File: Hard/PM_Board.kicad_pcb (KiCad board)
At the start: 2 copper layers, 70 x 70 mm, 75 parts, among them J1 Micro_SD_Card_Det_Hirose_DM3AT, J101 LiPo_V+, J102 LiPo_V-, J2 KRC_Conn_SWD, J3 USB_B_Micro, J4 KRC_Conn_CAN, J5 KRC_Conn_CAN, J6 KRC_Conn_CAN, Q1 SSM6J501NU, Q2 2n7002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

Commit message: [update] パターンを編集完了
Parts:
- moved C24 28.1 mm to (137.2, 90.4), turned to 180 degrees
- moved C15 26.1 mm to (148.3, 84.6)
- moved R8 26.1 mm to (156.1, 80.2)
- moved U2 26.1 mm to (150.6, 82.0)
- moved R9 26.1 mm to (156.1, 82.4)
- moved C16 26.1 mm to (154.6, 81.3)
- moved R10 26.1 mm to (157.8, 81.3)
- moved C25 18.9 mm to (138.8, 99.5), turned to 180 degrees
- moved C26 14.9 mm to (141.7, 103.5)
- moved D4 11.3 mm to (156.2, 88.5), turned to 270 degrees
- moved Q1 4.05 mm to (124.0, 106.5)
- moved Q2 4.05 mm to (130.9, 106.5)
- moved R13 4.05 mm to (126.6, 108.2)
- moved R14 4.05 mm to (132.4, 109.0)
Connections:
- C17 pad 1: Net-(C17-Pad1) -> VCC
- C19 pad 1: Net-(C17-Pad1) -> VCC
- J101 pad 1: Net-(D4-Pad2) -> +BATT
- Q1 pad 4: Net-(C17-Pad1) -> VCC
- Q1 pad 8: Net-(C17-Pad1) -> VCC
- R10 pad 1: VCC -> +BATT
- R10 pad 2: Net-(C17-Pad1) -> Net-(D4-Pad2)
- R13 pad 1: Net-(C17-Pad1) -> VCC
- R8 pad 1: VCC -> +BATT
- R9 pad 1: Net-(C17-Pad1) -> Net-(D4-Pad2)
- U2 pad 8: VCC -> +BATT
- VR1 pad 1: Net-(C17-Pad1) -> VCC
- VR1 pad 3: Net-(C17-Pad1) -> VCC
- VR2 pad 1: Net-(C17-Pad1) -> VCC
- VR2 pad 3: Net-(C17-Pad1) -> VCC
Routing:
- net Net-(C17-Pad1): track 54.4 -> 0.00 mm
- net VCC: track 116.9 -> 156.6 mm, vias 0 -> 2
- net /INA226_SCL: track 37.0 -> 51.0 mm
- net +BATT: track 0.00 -> 11.3 mm
- net +3V3: track 134.8 -> 144.6 mm
- net /INA226_SDA: track 38.5 -> 46.0 mm
- net /INA226_Alert: track 40.1 -> 45.5 mm
- net Net-(D4-Pad2): track 6.71 -> 1.40 mm
- net /Power_Cutoff: track 22.5 -> 18.6 mm, vias 2 -> 0
- net GND: vias 134 -> 138
- added copper zone on F.Cu, net +BATT
- removed copper zone on F.Cu, net Net-(C17-Pad1)

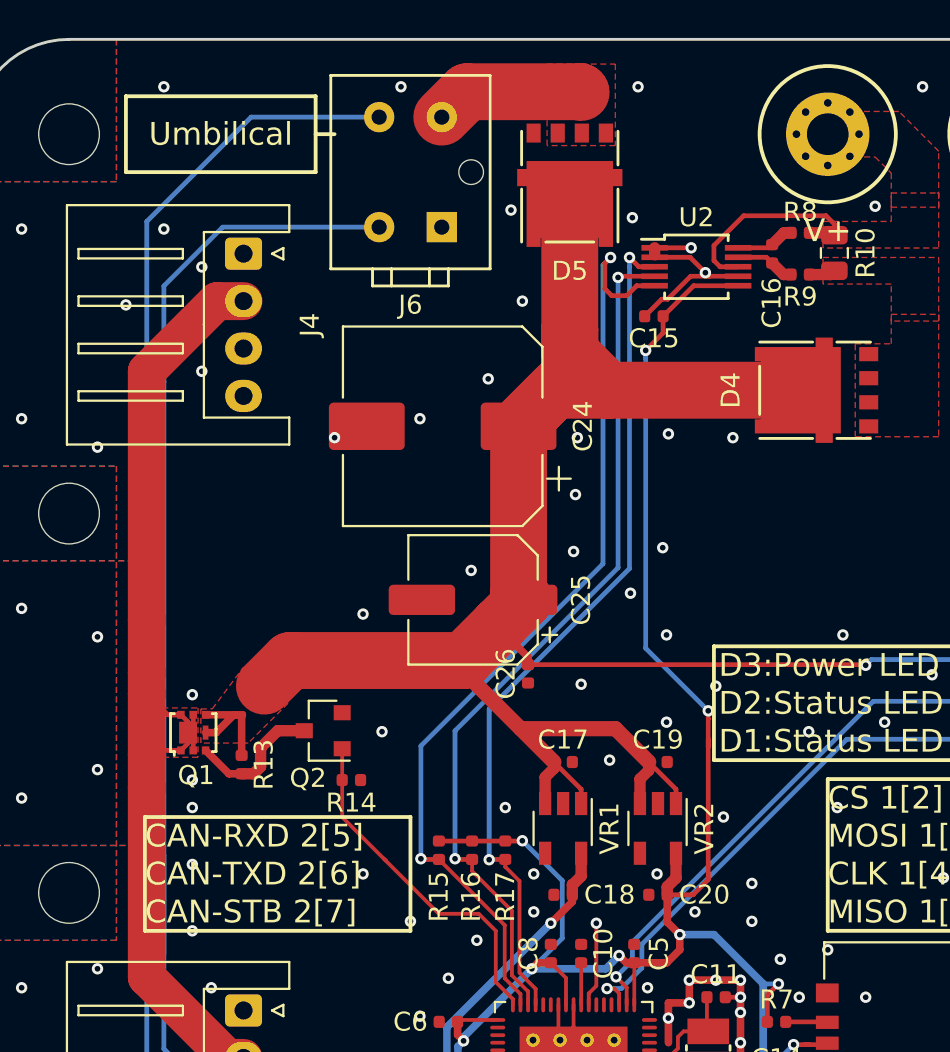
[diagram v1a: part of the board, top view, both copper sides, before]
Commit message: [update] アンビリカルをDF1Eに変更
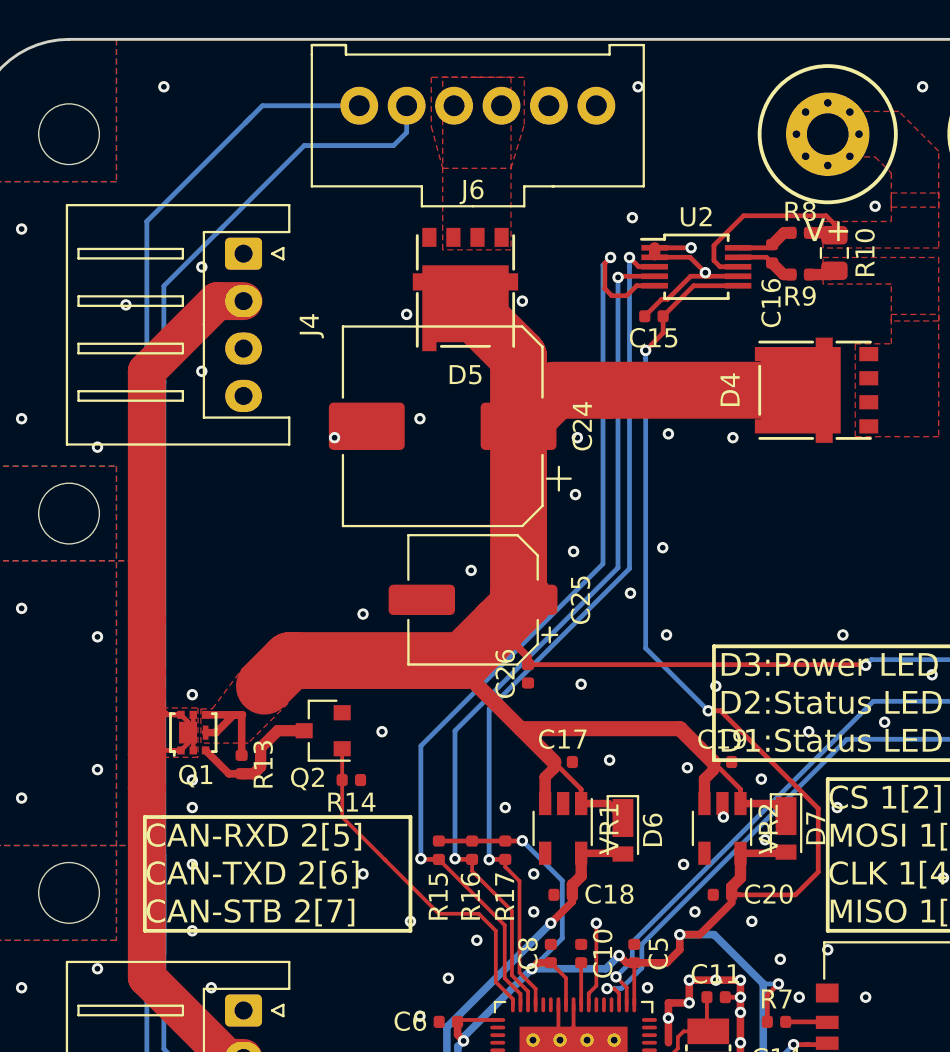
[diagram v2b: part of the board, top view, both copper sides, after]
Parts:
- added D6: RSX101VA, Diode_SMD:D_TUMD2, F.Cu at (146.7, 111.7)
- added D7: RSX101VA, Diode_SMD:D_TUMD2, F.Cu at (155.3, 111.6)
- J6: value KRC_Conn_CAN -> Umbilical; footprint KUTKiCad_footprint:Hirose_DF33-DF33C-4DP-3.3DSA_2x02_P3.3_Vertical -> KUTKiCad_footprint:Hirose_DF1E_DF1E-6P-2.5DS_1x06_P2.5mm_Vertical
- moved J6 10.4 mm to (145.3, 73.5), turned to 180 degrees
- moved D5 7.78 mm to (138.4, 83.9)
- moved C19 3.40 mm to (151.9, 108.1)
- moved C20 3.40 mm to (151.9, 115.1)
- moved VR2 3.40 mm to (151.9, 111.6)
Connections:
- J6 pad 2: Net-(D5-Pad2) -> GND
- J6 pad 3: /CAN_H -> Net-(D5-Pad2)
- J6 pad 4: /CAN_L -> Net-(D5-Pad2)
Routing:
- net +3V3: track 144.6 -> 153.0 mm
- net Net-(D5-Pad2): track 7.92 -> 0.00 mm
- net /CAN_H: track 77.2 -> 82.5 mm
- net +5V: track 22.9 -> 25.1 mm
- net VCC: track 156.6 -> 155.7 mm
- net GND: vias 138 -> 136
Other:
- board text removed: "Umbilical"

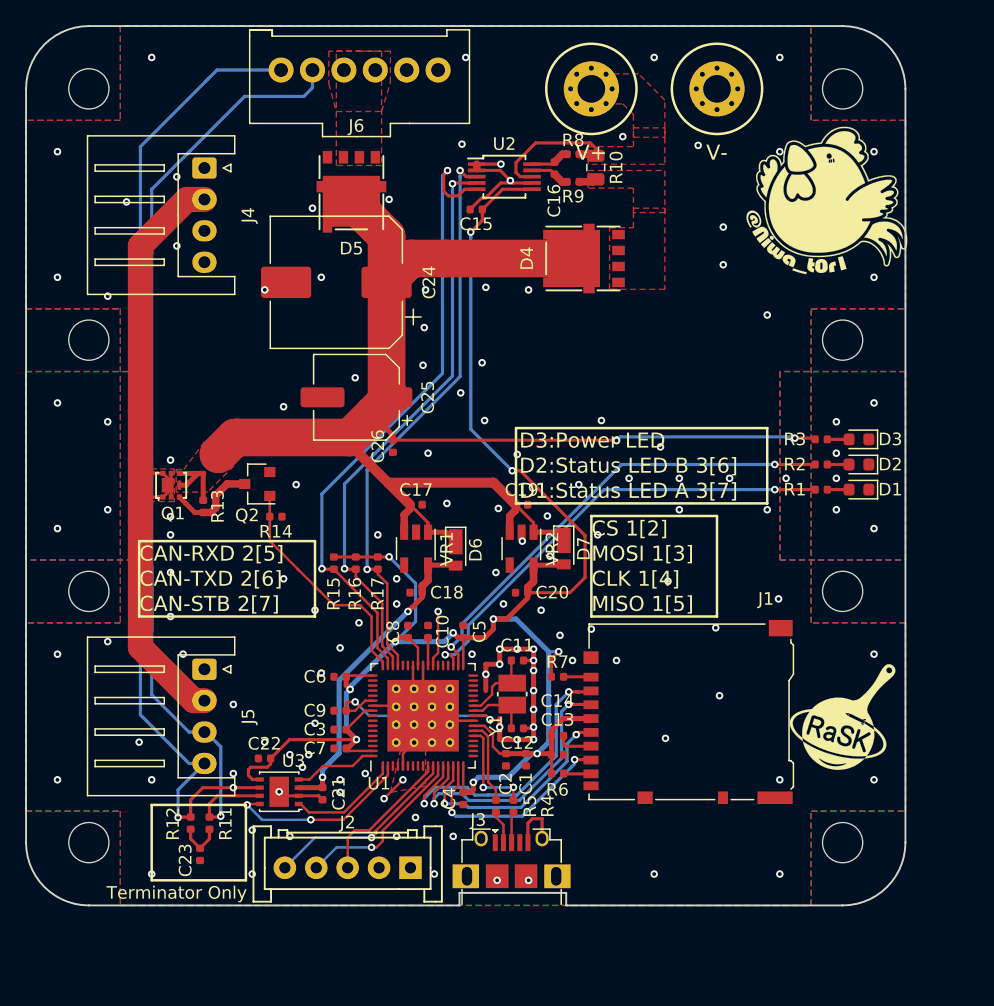
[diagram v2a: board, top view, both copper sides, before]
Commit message: [update] 部品の干渉を修正
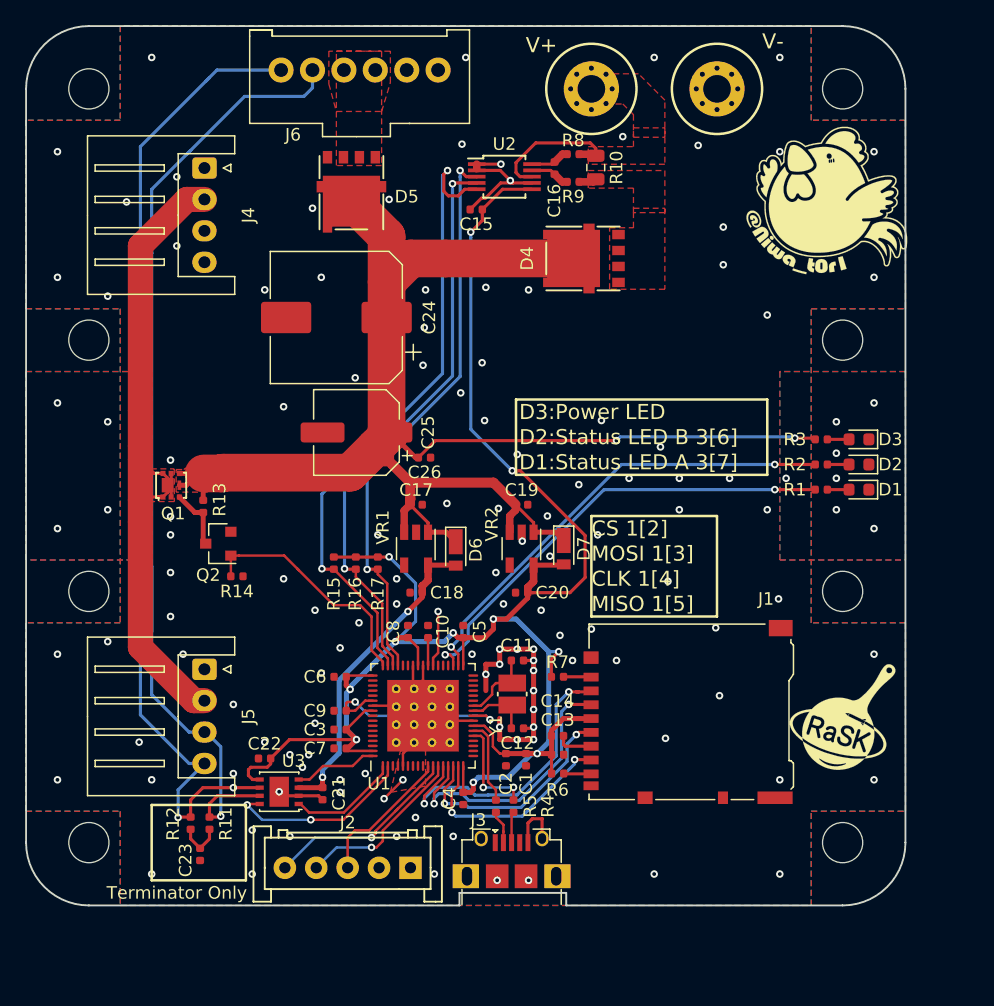
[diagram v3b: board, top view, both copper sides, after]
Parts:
- moved Q2 5.67 mm to (127.8, 111.2)
- moved R14 5.67 mm to (129.3, 113.8)
- moved C24 2.80 mm to (137.2, 93.2)
- moved C25 2.80 mm to (138.8, 102.3)
- moved C26 2.67 mm to (144.2, 104.3), turned to 180 degrees
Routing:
- net Net-(Q1-Pad3): track 7.24 -> 4.97 mm
- net /Power_Cutoff: track 18.6 -> 19.3 mm
- net GND: vias 136 -> 134
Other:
- board text removed: "CAN-RXD 2[5]"
- board text removed: "CAN-STB 2[7]"
- board text removed: "CAN-TXD 2[6]"

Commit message: [update] SDカード用のLDOを追加
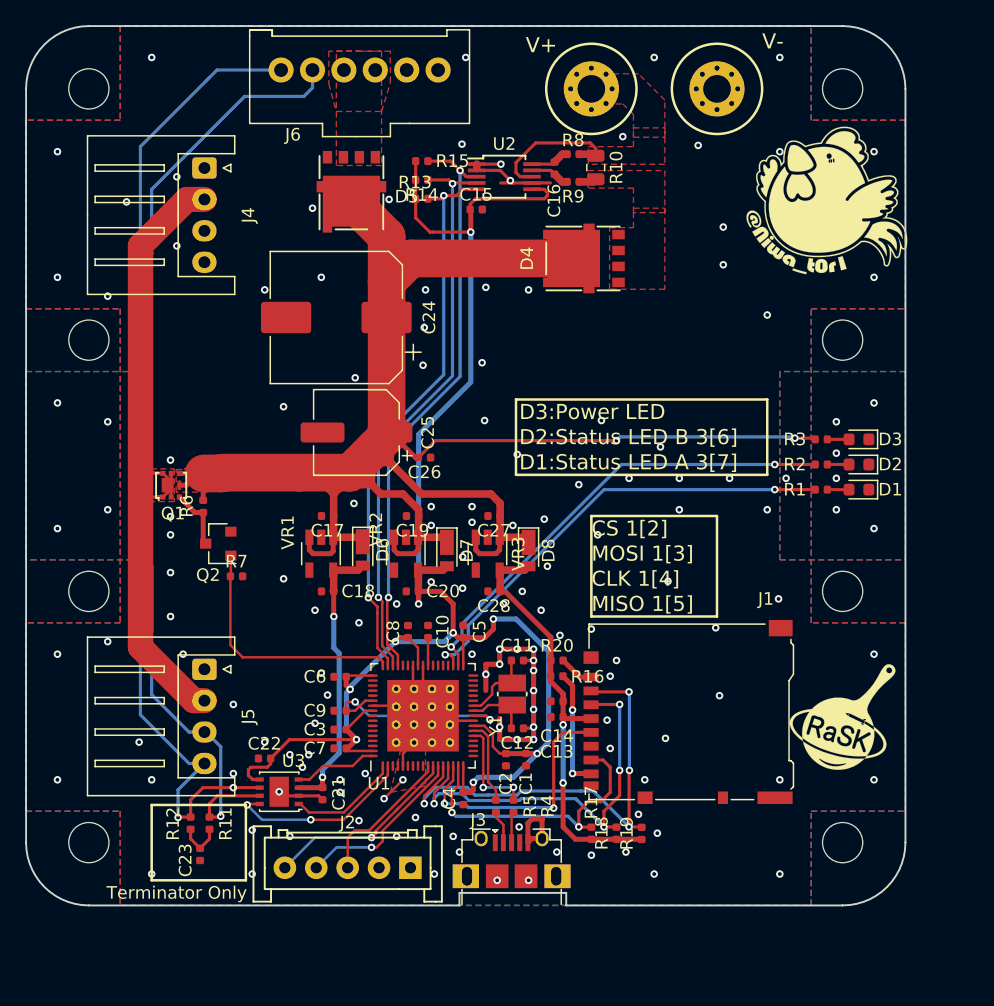
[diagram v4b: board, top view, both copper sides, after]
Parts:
- added C27: 1u, Capacitor_SMD:C_0402_1005Metric, F.Cu at (149.8, 109.0)
- added C28: 1u, Capacitor_SMD:C_0402_1005Metric, F.Cu at (149.8, 115.0)
- added D8: RSX101VA, Diode_SMD:D_TUMD2, F.Cu at (152.5, 111.8)
- added R18: 22k, Resistor_SMD:R_0402_1005Metric, F.Cu at (159.5, 134.2)
- added R19: 22k, Resistor_SMD:R_0402_1005Metric, F.Cu at (161.5, 134.3)
- added R20: 22k, Resistor_SMD:R_0402_1005Metric, F.Cu at (154.8, 120.5)
- added VR3: NCP718ASN330T1G, Package_TO_SOT_SMD:TSOT-23-5, F.Cu at (149.2, 112.0)
- R13, R14: value 1k -> 10k
- R16, R17: value 10k -> 22k
- R6, R7: value 47k -> 1k
- moved R6 35.3 mm to (126.6, 108.2), turned to 270 degrees
- moved R14 34.8 mm to (144.0, 82.2)
- moved R15 32.8 mm to (144.0, 80.8), turned to 0 degrees
- moved R13 30.0 mm to (144.0, 83.8), turned to 0 degrees
- moved R17 27.4 mm to (157.5, 134.2), turned to 90 degrees
- moved R7 26.8 mm to (129.2, 113.8)
- moved R16 18.4 mm to (154.8, 121.8), turned to 0 degrees
- moved D7 9.30 mm to (146.0, 111.8)
- moved VR2 9.21 mm to (142.8, 112.0)
- moved C19 8.73 mm to (143.3, 109.0), turned to 180 degrees
- moved C20 8.70 mm to (143.2, 115.0)
- moved VR1 7.56 mm to (136.0, 112.0)
- moved D6 7.40 mm to (139.3, 111.7)
- moved C17 7.11 mm to (136.5, 109.0), turned to 180 degrees
- moved C18 7.05 mm to (136.5, 115.0)
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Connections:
- net Net-(J3-Pad2) renamed /USB-
- net Net-(J3-Pad3) renamed /USB+
- C13 pad 1: +3V3 -> +3.3VP
- C14 pad 1: +3V3 -> +3.3VP
- J1 pad 4: +3V3 -> +3.3VP
- R13 pad 1: VCC -> +3V3
- R13 pad 2: Net-(Q1-Pad3) -> /INA226_SCL
- R14 pad 1: /Power_Cutoff -> +3V3
- R14 pad 2: GND -> /INA226_SDA
- R15 pad 2: /INA226_SCL -> /INA226_Alert
- R16 pad 1: +3V3 -> +3.3VP
- R16 pad 2: /INA226_SDA -> Net-(J1-Pad8)
- R17 pad 1: +3V3 -> +3.3VP
- R17 pad 2: /INA226_Alert -> /SD_MISO
- R6 pad 1: +3V3 -> VCC
- R6 pad 2: Net-(J1-Pad8) -> Net-(Q1-Pad3)
- R7 pad 1: +3V3 -> /Power_Cutoff
- R7 pad 2: Net-(J1-Pad1) -> GND
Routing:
- net +3.3VP: track 0.00 -> 34.2 mm, vias 0 -> 2
- net VCC: track 155.8 -> 182.9 mm
- net +3V3: track 153.0 -> 138.9 mm, vias 11 -> 9
- net /SD_CS: track 24.0 -> 37.1 mm, vias 2 -> 4
- net /SD_MOSI: track 22.1 -> 32.4 mm, vias 2 -> 4
- net Net-(J1-Pad8): track 2.19 -> 9.55 mm, vias 0 -> 2
- net /SD_MISO: track 17.2 -> 23.6 mm
- net /INA226_SCL: track 51.0 -> 44.7 mm
- net Net-(U1-Pad41): track 4.47 -> 0.00 mm, vias 1 -> 0
- net /SD_CLK: track 18.4 -> 21.6 mm
- net +5V: track 25.1 -> 22.3 mm
- net GND: track 56.1 -> 53.4 mm, vias 134 -> 148
- net /INA226_Alert: track 45.5 -> 46.6 mm
- net /Power_Cutoff: track 19.3 -> 20.1 mm
- net /INA226_SDA: track 46.0 -> 45.3 mm
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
